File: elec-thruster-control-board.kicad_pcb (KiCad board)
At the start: 2 copper layers, 70 x 69 mm, 50 parts, among them J1 gp0-pwm0A, J10 gp17-pwm0B, J11 Conn_01x06, J12 Conn_01x06, J13 Conn_01x07, J2 gp2-pwm1A, J3 gp4-pwm2A, J4 gp6-pwm3A, J5 gp8-pwm4A, J6 gp27-pwm5B, J7 gp26-pwm5A, J8 gp21-pwm2B, J9 gp19-pwm1B

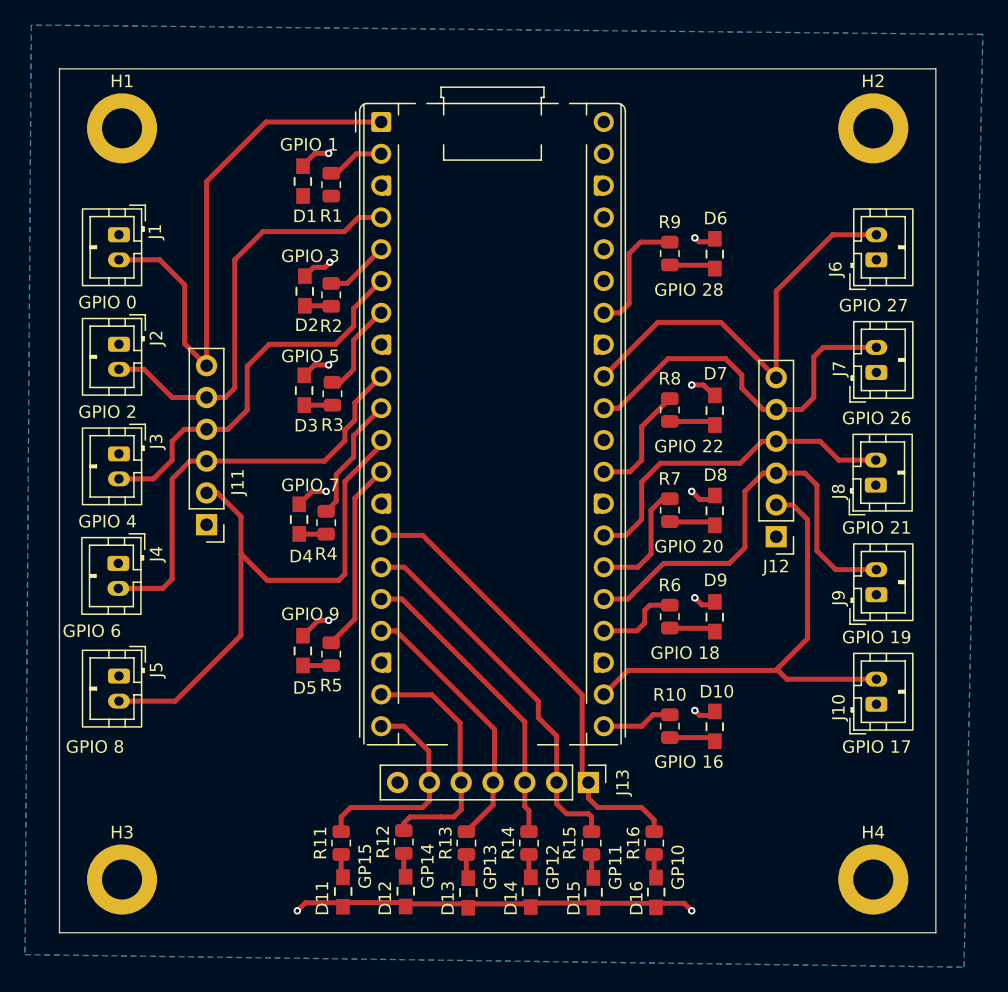
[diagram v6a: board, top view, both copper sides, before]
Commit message: Tightened spacing on both side of board should save ~6.5mm in width if 5mm gap between header and connector. Can save ~10.5mm if 3mm gap between header and connector. Wire connection still incomplete TBD between 5mm gap and 3mm gap.
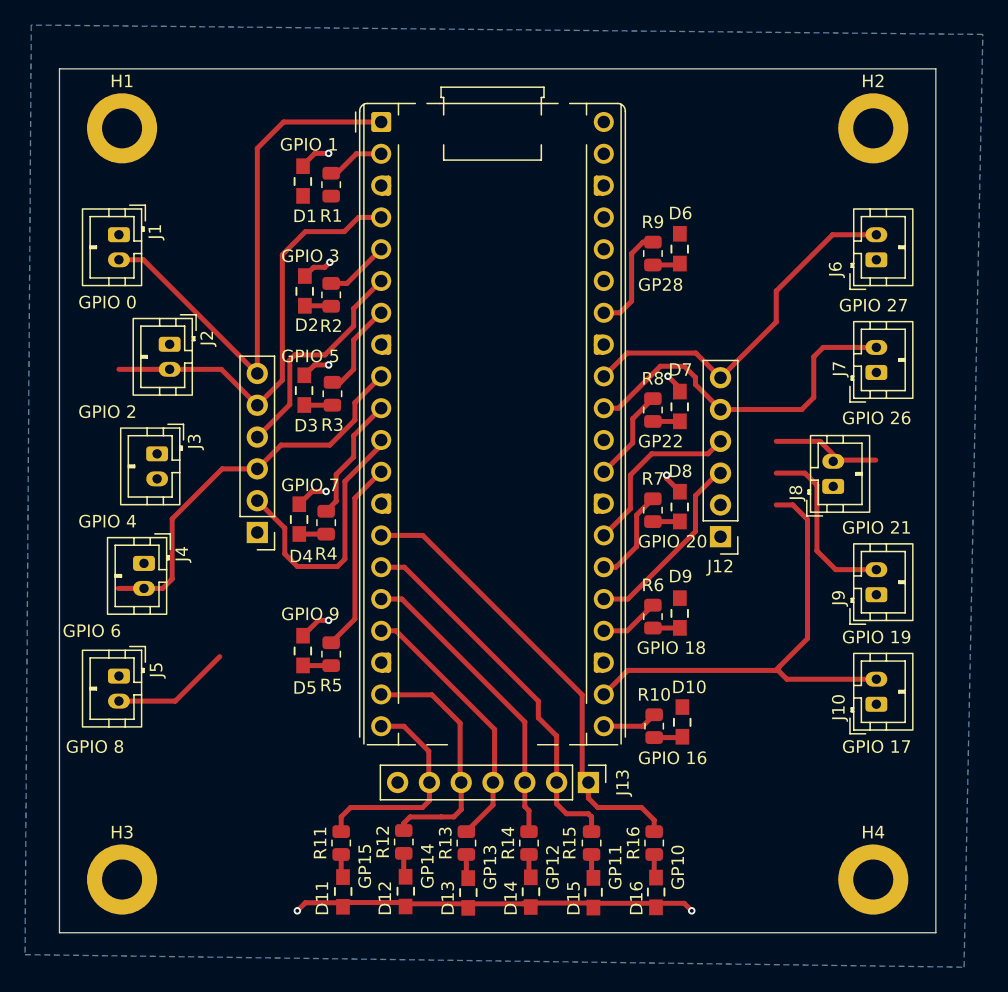
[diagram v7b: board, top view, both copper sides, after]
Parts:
- moved J12 4.45 mm to (157.8, 84.1)
- moved J11 4.10 mm to (120.8, 83.8)
- moved J2 4.05 mm to (113.8, 68.8)
- moved J8 3.40 mm to (166.8, 80.1)
- moved J3 3.05 mm to (112.8, 77.5)
- moved D6 2.83 mm to (154.7, 61.1)
- moved D7 2.82 mm to (154.7, 73.7)
- moved D8 2.82 mm to (154.7, 81.7)
- moved D9 2.82 mm to (154.7, 90.2)
- moved D10 2.62 mm to (154.9, 98.9)
- moved J4 2.05 mm to (111.8, 86.2)
- moved R6 1.35 mm to (152.4, 90.5)
- moved R7 1.35 mm to (152.4, 82.0)
- moved R8 1.35 mm to (152.4, 74.0)
- moved R9 1.35 mm to (152.4, 61.5)
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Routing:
- net /gp8-pwm4A: track 46.2 -> 30.9 mm
- net /gp4-pwm2A: track 31.2 -> 18.0 mm
- net GND: track 55.5 -> 48.3 mm, vias 12 -> 9
- net /gp19-pwm1B: track 35.1 -> 29.5 mm
- net /gp27-pwm5B: track 34.2 -> 29.5 mm
- net /gp21-pwm2B: track 27.2 -> 22.6 mm
- net /gp6-pwm3A: track 34.5 -> 32.1 mm
- net Net-(D9-A): track 4.26 -> 2.20 mm
- net Net-(A1-GPIO18): track 6.71 -> 4.77 mm
- net Net-(A1-GPIO20): track 9.59 -> 7.66 mm
- net Net-(A1-GPIO22): track 9.25 -> 7.47 mm
- net Net-(D8-A): track 3.76 -> 2.16 mm
- net Net-(D7-A): track 3.76 -> 2.16 mm
- net Net-(D6-A): track 3.76 -> 2.16 mm
- net Net-(A1-GPIO28_ADC2): track 9.95 -> 8.49 mm
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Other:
- board text added: "GP22"
- board text added: "GP28"
- board text removed: "GPIO 22"
- board text removed: "GPIO 28"

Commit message: Finished the job for Kekoa's compression
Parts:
- moved J10 8.28 mm to (162.8, 101.0)
- moved J9 7.83 mm to (162.8, 91.0)
- moved J6 7.62 mm to (162.7, 61.0)
- moved J7 7.55 mm to (162.7, 71.2)
- moved J5 7.43 mm to (116.3, 98.8)
- moved H2 7.25 mm to (162.8, 51.2)
- moved H4 7.25 mm to (162.8, 111.5)
- moved J1 6.67 mm to (116.3, 58.8)
- moved H1 6.01 mm to (116.0, 51.2)
- moved H3 6.00 mm to (116.0, 111.5)
- moved J4 5.15 mm to (116.2, 88.8)
- moved J8 4.15 mm to (162.8, 81.0)
- moved J3 3.67 mm to (116.2, 78.8)
- moved J2 2.50 mm to (116.3, 68.8)
- moved J12 0.50 mm to (158.3, 84.1)
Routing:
- net /gp8-pwm4A: track 30.9 -> 42.5 mm
- net /gp0-pwm0A: track 43.6 -> 34.1 mm
- net /gp4-pwm2A: track 18.0 -> 26.5 mm
- net /gp26-pwm5A: track 28.9 -> 21.0 mm
- net /gp2-pwm1A: track 34.2 -> 27.7 mm
- net /gp17-pwm0B: track 38.9 -> 33.6 mm
- net /gp21-pwm2B: track 22.6 -> 20.0 mm
- net /gp6-pwm3A: track 32.1 -> 29.8 mm
- net /gp27-pwm5B: track 29.5 -> 28.6 mm
- net /gp19-pwm1B: track 29.5 -> 30.0 mm
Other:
- board size 70 x 69 mm -> 55.8 x 69.5 mm
- board text added: "GP16"
- board text added: "GP18"
- board text added: "GP20"
- board text removed: "GPIO 16"
- board text removed: "GPIO 18"
- board text removed: "GPIO 20"
